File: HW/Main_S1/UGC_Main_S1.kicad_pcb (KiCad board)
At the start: 4 copper layers, 125.7 x 76.4 mm, 134 parts, among them J1 SM02B-SURS-TF_LF__SN_, J10 SM02B-SURS-TF_LF__SN_, J13 503480-0640, J2 503480-0640, J4 Conn_01x06_Pin, J5 UJ31-CH-G1-SMT-TR, J6 Trigger, J7 Trigger, J8 Conn_01x02, J9 Conn_01x02, Q3 BSS138DW, Q4 BSS138DW, Q5 MMBT2222A, Q6 MMBT2222A, SW1 SW_Push, SW10 SW_Push, SW11 SW_Push, SW12 SW_Push, SW13 SW_Push, SW14 SW_TS-1187A, SW15 1TS026A-1000-0550, SW17 SW_TS-1187A, SW18 SW_TS-1187A, SW19 SW_TS-1187A, SW2 SW_Push, SW3 SW_Push, SW4 SW_Push, SW5 SW_TS-1187A, SW6 GL18_SW, SW7 SW_Push, SW8 SW_Push, SW9 SW_TS-1187A, U10 ST_LSM6, U4 TPS630001RCR, U6 MCP3002, U7 MCP3002, U8 RP2040, U9 GD25Q80EEIGR, X1 ModConnect, X2 ModConnect, X3 ModConnect, X4 ModConnect, X5 ModConnect, X6 ModConnect, Y1 ABM8-272-T3

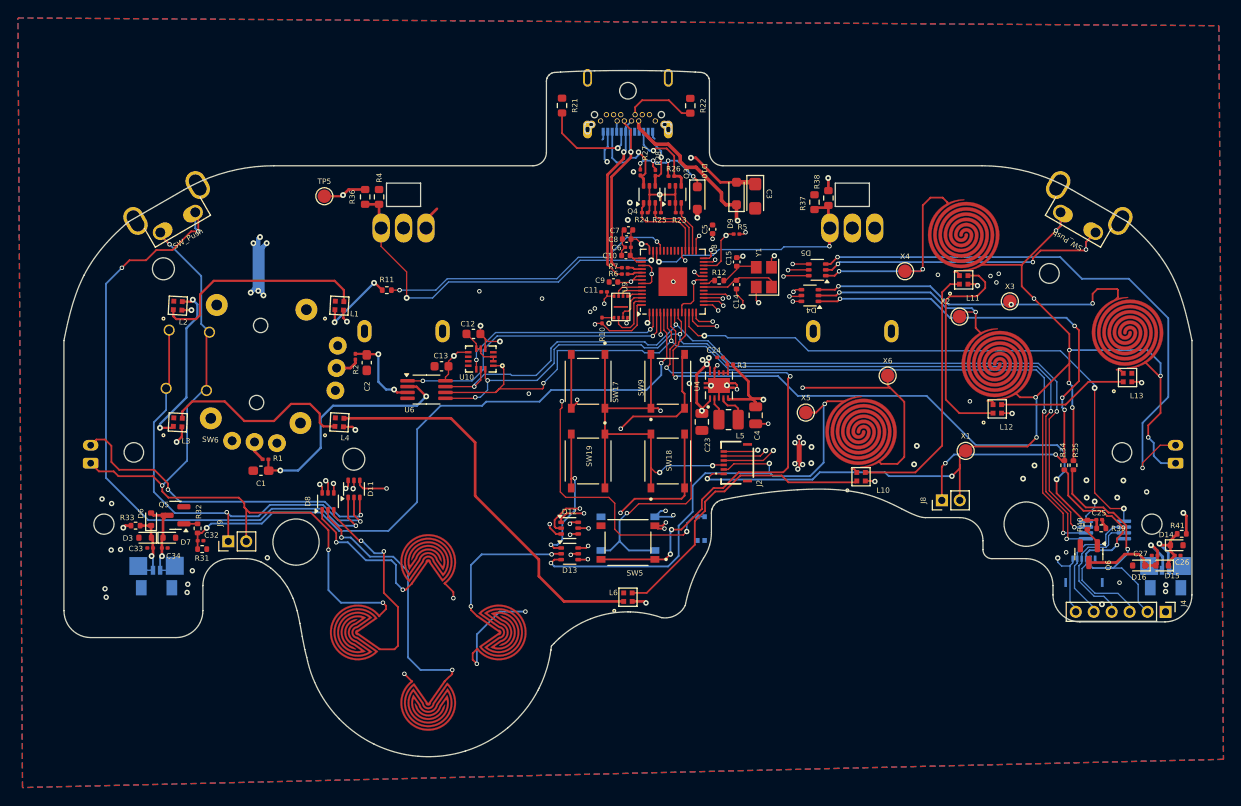
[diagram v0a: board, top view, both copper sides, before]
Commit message: Update PCBs
- Fix BOMs so they reference real part numbers
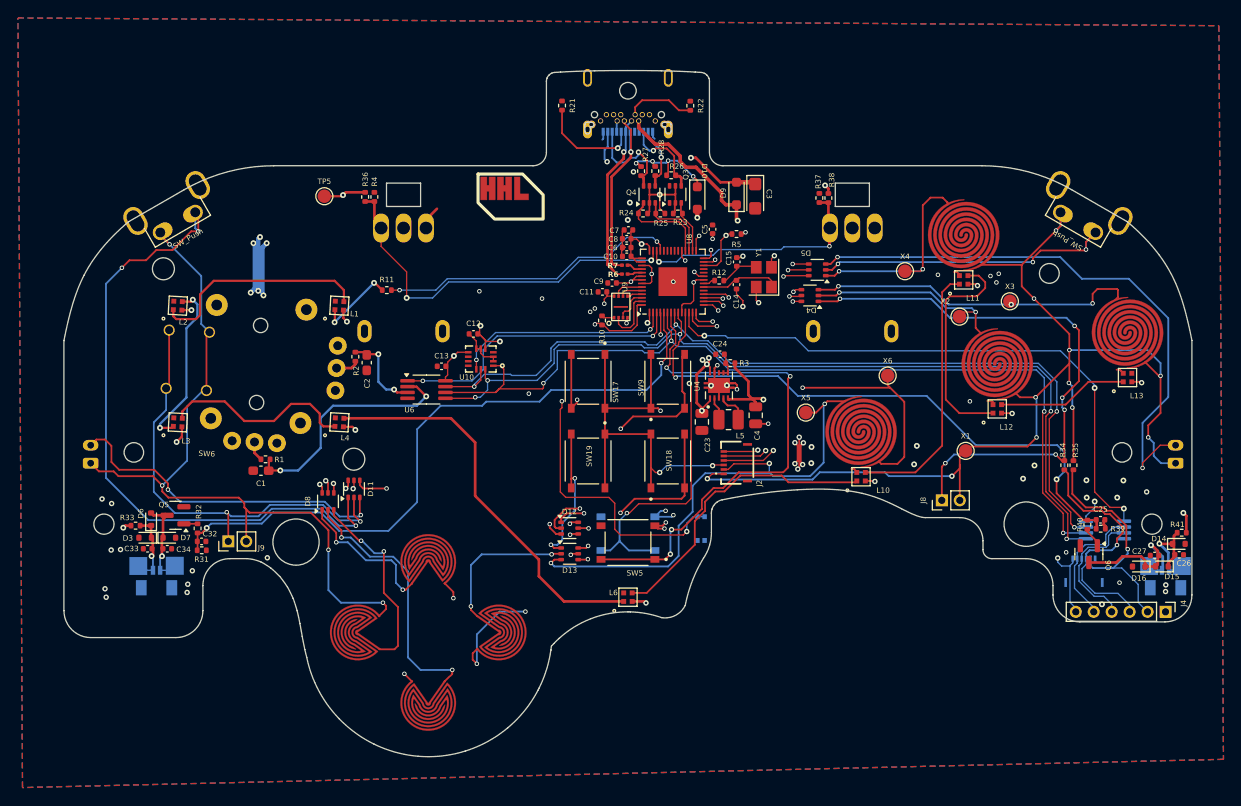
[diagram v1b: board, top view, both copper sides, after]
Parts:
- added REF**: HHL_Logo, hhl:HHL_Logo, F.Cu at (204.7, 98.4)
- C1, C2: value .047u -> 47nF
- C10, C5, C7, C9: value 100n -> 100nF
- C11, C24, C6: value 100n -> 100nF; footprint Capacitor_SMD:C_0201_0603Metric -> Capacitor_SMD:C_0402_1005Metric
- C12, C13: footprint Capacitor_SMD:C_0603_1608Metric -> Capacitor_SMD:C_0402_1005Metric
- C14, C15: value 15p -> 15pF
- C25, C32: footprint Capacitor_SMD:C_0201_0603Metric -> Capacitor_SMD:C_0402_1005Metric
- C26, C27, C33, C34: value 1u -> 1uF; footprint Capacitor_SMD:C_0201_0603Metric -> Capacitor_SMD:C_0402_1005Metric
- C3: value 47uF 6.3v -> 47uF
- C8: value 1u -> 1uF
- R1, R10, R2, R23, R24, R25, R26, R27, R28, R5: footprint Resistor_SMD:R_0201_0603Metric -> Resistor_SMD:R_0402_1005Metric
- R11: value 330 -> 330R
- R21, R22: value 5.1kohm -> 5.1k; footprint Resistor_SMD:R_0603_1608Metric -> Resistor_SMD:R_0402_1005Metric
- R3: value 100 -> 100R; footprint Resistor_SMD:R_0201_0603Metric -> Resistor_SMD:R_0402_1005Metric
- R36, R37, R38, R4: footprint Resistor_SMD:R_0603_1608Metric -> Resistor_SMD:R_0402_1005Metric
- R6, R7: value 27 -> 27R
- moved R37 0.72 mm to (239.8, 98.1)
- moved R4 0.52 mm to (190.2, 98.0)
- moved C24 0.35 mm to (228.7, 115.5)
- moved C33 0.30 mm to (165.0, 137.2)
- moved C34 0.29 mm to (167.2, 137.2)
- moved D14 0.28 mm to (279.9, 136.6)
- moved R7 0.28 mm to (218.1, 105.6)
- moved R25 0.27 mm to (222.1, 99.8)
- moved R24 0.23 mm to (220.2, 99.8)
- moved R28 0.22 mm to (221.5, 95.1)
- moved C26 0.19 mm to (279.9, 137.8)
- moved C9 0.19 mm to (216.7, 107.6)
- moved C11 0.18 mm to (215.6, 108.5)
- moved R27 0.18 mm to (219.9, 95.1)
- moved C6 0.15 mm to (218.3, 103.6)
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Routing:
- net N_CLOCK_3.3: track 9.57 -> 10.2 mm
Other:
- board text added: "GCU S1 Designed by Mitch 10.25.2024"
- board text removed: "GCU S1 Designed by Mitch"

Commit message: Update PCB directory
Accessory boards have been migrated to Open-GC-Ultimate
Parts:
- removed SW15: 1TS026A-1000-0550, hhl:1TS026A-1000-0550
- added U1: ST_LSM6, hhl:LGA14, F.Cu at (206.8, 114.8)
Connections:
- SW14 pad C: RP_RUN -> USB_BOOT
- SW14 pad D: RP_RUN -> USB_BOOT
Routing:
- net RP_RUN: track 62.1 -> 5.95 mm, vias 3 -> 0
- net IMU1_CS: track 2.48 -> 20.3 mm, vias 1 -> 2
- net GND: track 41.3 -> 48.7 mm, vias 54 -> 57
- net +3V3: track 120.4 -> 126.6 mm
- net SPI_RX: track 101.0 -> 104.6 mm
- net USB_BOOT: track 50.1 -> 46.9 mm
- net SPI_TX: track 99.8 -> 102.9 mm, vias 5 -> 6
- net SPI_CK: track 97.7 -> 100.2 mm, vias 4 -> 5
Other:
- board text added: "GCU S1 Designed by Mitch 10.29.2024"
- board text removed: "GCU S1 Designed by Mitch 10.25.2024"

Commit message: Update S1
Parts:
- removed U6, U7: MCP3002, Package_SO:MSOP-8_3x3mm_P0.65mm
- added C16: 100nF, Capacitor_SMD:C_0402_1005Metric, F.Cu at (207.0, 111.8)
- added S7: TMUX1204DQAR, hhl:TMUX1204DQAR, F.Cu at (210.0, 110.5)
- L1, L10, L11, L12, L13, L2, L3, L4, L6: value SK6805-EC-15 -> SK6805-EC-10; footprint hhl:SK6805-EC-15 -> hhl:SK6805-EC-10
- SW14, SW17, SW18, SW19, SW5, SW9: value SW_TS-1187A -> TS-1187A-C-A-B
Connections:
- U8 pad 12: RADC_CS -> unconnected-(U8-GPIO9-Pad12)
- U8 pad 3: LADC_CS -> unconnected-(U8-GPIO1-Pad3)
- U8 pad 34: I2C_SDA -> unconnected-(U8-GPIO22-Pad34)
- U8 pad 35: I2C_SCL -> ADC_ADDR_0
- U8 pad 36: USB_EN -> ADC_ADDR_1
- U8 pad 37: USB_SEL -> unconnected-(U8-GPIO25-Pad37)
- U8 pad 38: ESP_EN -> ADC_MUX_OUT
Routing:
- net RY: track 15.0 -> 89.5 mm, vias 0 -> 4
- net RX: track 15.1 -> 88.0 mm, vias 0 -> 4
- net SPI_RX: track 104.6 -> 32.8 mm, vias 4 -> 2
- net SPI_TX: track 102.9 -> 31.7 mm, vias 6 -> 3
- net SPI_CK: track 100.2 -> 33.0 mm, vias 5 -> 3
- net RADC_CS: track 66.8 -> 0.00 mm, vias 3 -> 0
- net LADC_CS: track 33.5 -> 0.00 mm, vias 2 -> 0
- net ADC_ADDR_0: track 0.00 -> 25.5 mm, vias 0 -> 2
- net ADC_MUX_OUT: track 0.00 -> 23.8 mm, vias 0 -> 2
- net ADC_ADDR_1: track 0.00 -> 23.3 mm, vias 0 -> 2
- net LY: track 9.54 -> 31.3 mm
- net LX: track 26.8 -> 45.1 mm
- net unconnected-(U8-GPIO1-Pad3): track 0.00 -> 2.79 mm, vias 0 -> 1
- net I: track 154.6 -> 152.5 mm
- net GND: track 48.7 -> 50.5 mm, vias 57 -> 77
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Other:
- board text added: "GCU S1 Designed by Mitch 11.12.2024"
- board text removed: "GCU S1 Designed by Mitch 10.29.2024"

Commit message: S1 ESD
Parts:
- added U2: USBLC6-2P6, Package_TO_SOT_SMD:SOT-666, F.Cu at (216.4, 97.9)
- added U3: USBLC6-2P6, Package_TO_SOT_SMD:SOT-666, F.Cu at (211.8, 95.4)
- added U5: USBLC6-2P6, Package_TO_SOT_SMD:SOT-666, F.Cu at (214.1, 95.4)
- D10, D9: value CUS08F30 -> CUS08F30,H3F
- moved R7 0.17 mm to (218.1, 105.8)
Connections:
- Q3 pad 4: N_LATCH -> N_LATCH_SAFE
- Q4 pad 4: N_DATA -> N_DATA_SAFE
- Q4 pad 6: N_CLOCK -> N_CLOCK_SAFE
- R26 pad 2: N_LATCH -> N_LATCH_SAFE
- R27 pad 2: N_CLOCK -> N_CLOCK_SAFE
- R28 pad 2: N_DATA -> N_DATA_SAFE
- R6 pad 1: D+ -> SAFE_D+
- R7 pad 1: D- -> SAFE_D-
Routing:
- net N_LATCH_SAFE: track 0.00 -> 16.8 mm, vias 0 -> 2
- net VBUS_SYS: track 63.7 -> 79.9 mm, vias 2 -> 3
- net N_DATA_SAFE: track 0.00 -> 14.9 mm, vias 0 -> 2
- net D+: track 19.2 -> 8.80 mm
- net D-: track 20.5 -> 10.9 mm
- net N_CLOCK_SAFE: track 0.00 -> 9.47 mm, vias 0 -> 2
- net SAFE_D+: track 0.00 -> 9.00 mm
- net SAFE_D-: track 0.00 -> 8.06 mm
- net N_DATA: track 15.8 -> 21.9 mm
- net +3V3_PRE: track 27.0 -> 30.5 mm
- net GND: track 50.5 -> 53.8 mm, vias 77 -> 78
- net N_LATCH: track 16.7 -> 19.7 mm
- net SHARED_PU: track 11.8 -> 10.6 mm, vias 4 -> 2
- net N_CLOCK: track 16.1 -> 15.4 mm, vias 1 -> 2
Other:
- board text added: "GCU S1 Designed by Mitch 2.5.2025"
- board text removed: "GCU S1 Designed by Mitch 11.12.2024"
